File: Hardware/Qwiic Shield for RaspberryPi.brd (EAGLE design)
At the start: 65 x 30.5 mm, 24 parts, among them J1 Qwiic Right Angle, J10 RASPBERRYPI-40-PIN-GPIO_PTH_N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, J6 Qwiic Right Angle, J7 Qwiic Right Angle, J8 Qwiic Right Angle, U2 3.3V/600mA

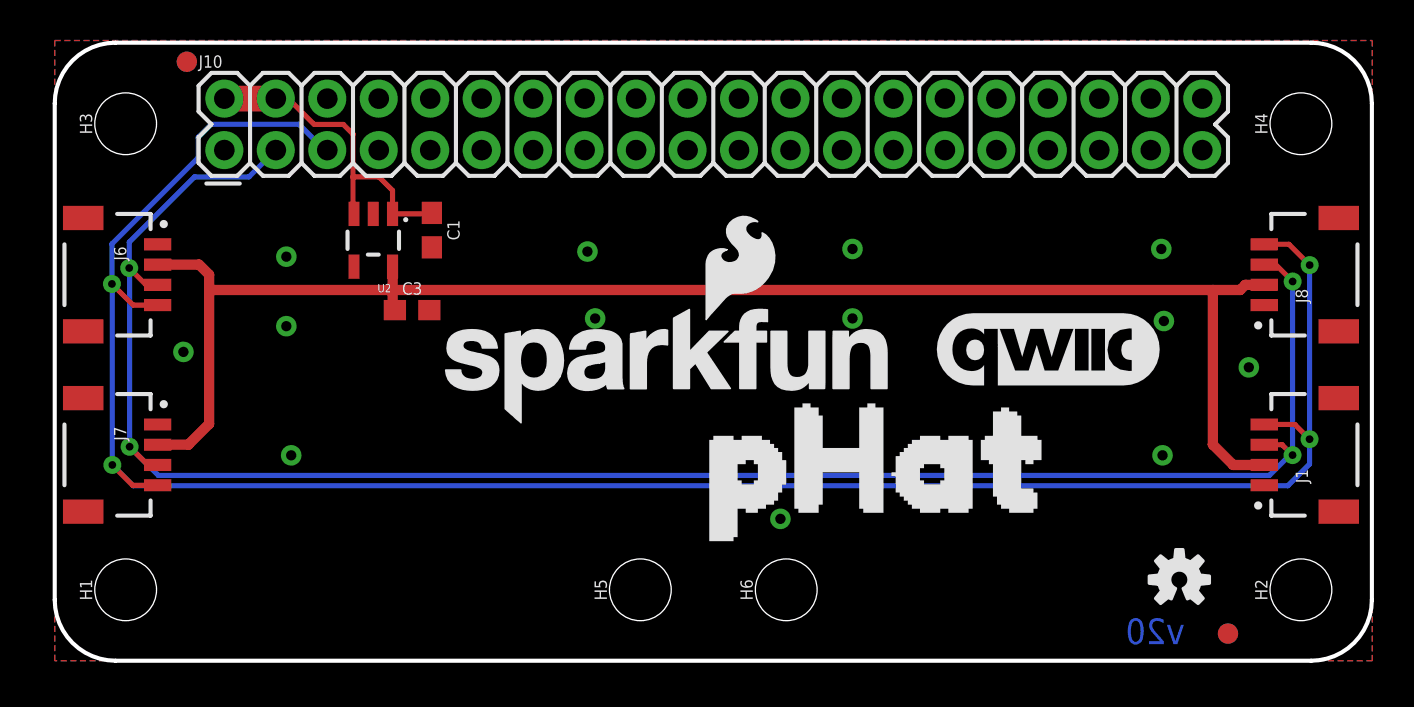
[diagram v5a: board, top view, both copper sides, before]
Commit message: Adds I2C pullup resistors
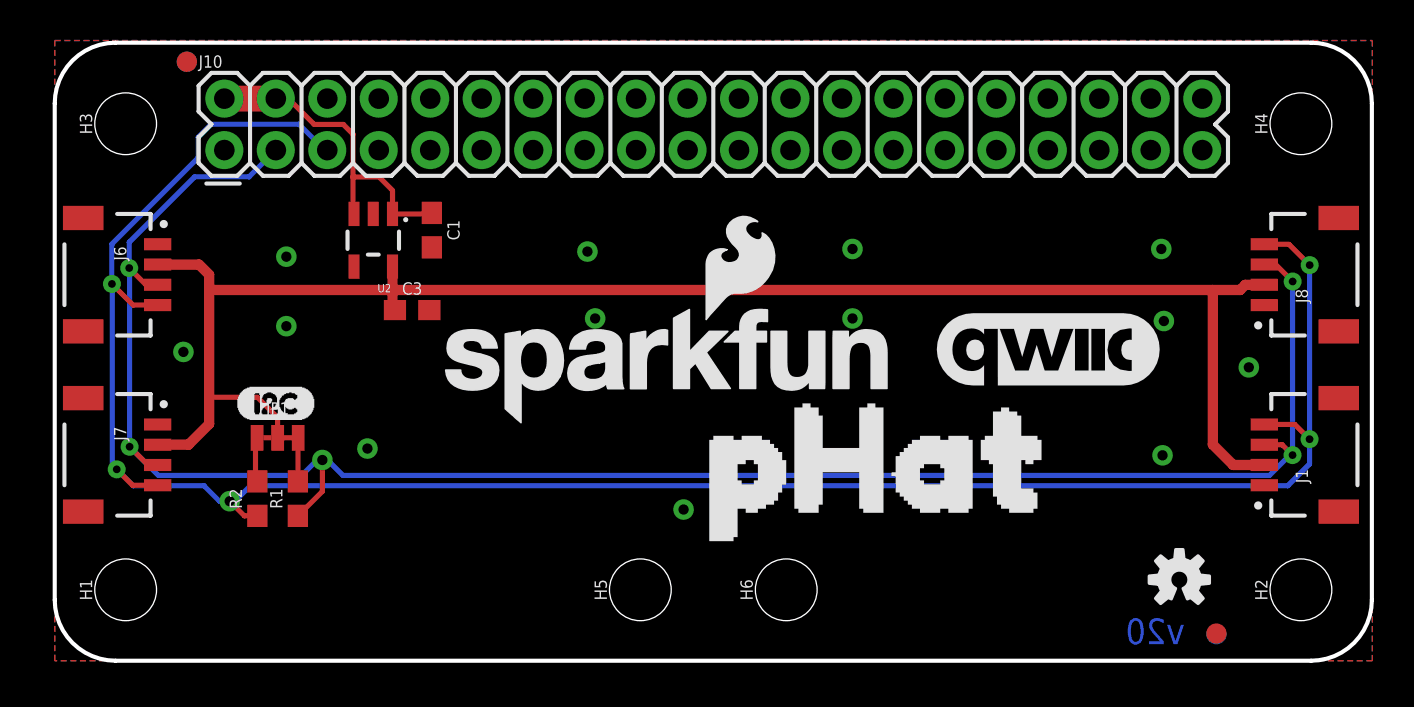
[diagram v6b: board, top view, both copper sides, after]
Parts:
- added JP1: PULLUP, SparkFun-Jumpers:SMT-JUMPER_3_2-NC_TRACE_NO-SILK
- added R1, R2: 2.2k, SparkFun-Resistors:0603
- added U$2: (no value), Labels:I2C-()
- moved FD3 0.57 mm to (57.3, 1.31)
- moved FD2 0.57 mm to (57.3, 1.34)
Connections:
- new net N$3: JP1.3, R1.2
- new net N$4: JP1.1, R2.2
- net 3.3V: now also JP1.2
- net SCL: now also R2.1
- net SDA: now also R1.1
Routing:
- net 3.3V: track 78.0 -> 82.8 mm
- net SDA: track 93.0 -> 97.1 mm, vias 4 -> 5
- net N$3: track 0.00 -> 2.57 mm
- net N$4: track 0.00 -> 2.32 mm
- net SCL: track 105.4 -> 107.4 mm, vias 4 -> 5
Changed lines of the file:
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@@
 <setting verticaltext="up"/>
 </settings>
-<grid distance="1" unitdist="mm" unit="mm" style="lines" multiple="1" display="yes" altdistance="0.01" altunitdist="mm" altunit="mm"/>
+<grid distance="0.1" unitdist="inch" unit="inch" style="lines" multiple="1" display="yes" altdistance="0.01" altunitdist="inch" altunit="inch"/>
 <layers>
 <layer number="1" name="Top" color="4" fill="1" visible="yes" active="yes"/>
@@
 </element>
 <element name="FD1" library="SparkFun-Aesthetics" package="FIDUCIAL-1X2" value="FIDUCIAL1X2" x="6.52" y="29.56" smashed="yes" rot="R180"/>
-<element name="FD2" library="SparkFun-Aesthetics" package="FIDUCIAL-1X2" value="FIDUCIAL1X2" x="57.9" y="1.34" smashed="yes" rot="R180"/>
+<element name="FD2" library="SparkFun-Aesthetics" package="FIDUCIAL-1X2" value="FIDUCIAL1X2" x="57.33" y="1.34" smashed="yes" rot="R180"/>
 <element name="J1" library="SparkFun-Connectors" package="JST04_1MM_RA" value="Qwiic Right Angle" x="59.68988125" y="10.16078125" smashed="yes" rot="R90">
 <attribute name="NAME" x="61.84888125" y="8.76378125" size="0.6096" layer="25" font="vector" ratio="20" rot="R90"/>
@@
 <attribute name="VALUE" x="62.992" y="17.399" size="0.6096" layer="27" font="vector" ratio="20" rot="R90"/>
 </element>
-<element name="FD3" library="SparkFun-Aesthetics" package="FIDUCIAL-1X2" value="FIDUCIAL1X2" x="57.9" y="1.34" smashed="yes" rot="MR0"/>
+<element name="FD3" library="SparkFun-Aesthetics" package="FIDUCIAL-1X2" value="FIDUCIAL1X2" x="57.33" y="1.31" smashed="yes" rot="MR0"/>
 <element name="FD4" library="SparkFun-Aesthetics" package="FIDUCIAL-1X2" value="FIDUCIAL1X2" x="6.52" y="29.56" smashed="yes" rot="MR0"/>
 <element name="LOGO2" library="SparkFun-Aesthetics" package="REVISION" value="REVISION" x="2.54" y="-26.67" smashed="yes"/>
@@
 <element name="LOGO3" library="SparkFun-Aesthetics" package="OSHW-LOGO-S" value="OSHW-LOGOS" x="55.5" y="4" smashed="yes"/>
 <element name="U$3" library="MicroPiHat" package="PHAT0" value="" x="27.5" y="10" smashed="yes"/>
+<element name="JP1" library="SparkFun-Jumpers" package="SMT-JUMPER_3_2-NC_TRACE_NO-SILK" value="PULLUP" x="11" y="11" smashed="yes">
+<attribute name="NAME" x="11" y="12.143" size="0.6096" layer="25" font="vector" ratio="20" align="bottom-center"/>
+<attribute name="VALUE" x="11" y="9.857" size="0.6096" layer="27" font="vector" ratio="20" align="top-center"/>
+</element>
+<element name="R1" library="SparkFun-Resistors" package="0603" value="2.2k" x="12" y="8" smashed="yes" rot="R90">
+<attribute name="NAME" x="11.238" y="8" size="0.6096" layer="25" font="vector" ratio="20" rot="R90" align="bottom-center"/>
+<attribute name="PROD_ID" value="RES-08272" x="12" y="8" size="1.778" layer="27" font="vector" ratio="15" rot="R90" display="off"/>
+<attribute name="VALUE" x="12.762" y="8" size="0.6096" layer="27" font="vector" ratio="20" rot="R90" align="top-center"/>
+</element>
+<element name="R2" library="SparkFun-Resistors" package="0603" value="2.2k" x="10" y="8" smashed="yes" rot="R90">
+<attribute name="NAME" x="9.238" y="8" size="0.6096" layer="25" font="vector" ratio="20" rot="R90" align="bottom-center"/>
+<attribute name="PROD_ID" value="RES-08272" x="10" y="8" size="1.778" layer="27" font="vector" ratio="15" rot="R90" display="off"/>
+<attribute name="VALUE" x="10.762" y="8" size="0.6096" layer="27" font="vector" ratio="20" rot="R90" align="top-center"/>
+</element>
+<element name="U$2" library="Labels" package="I2C-()" value="" x="8.89" y="12.7" smashed="yes"/>
 </elements>
 <signals>
@@
 <via x="39.37" y="16.891" extent="1-16" drill="0.508"/>
 <via x="39.37" y="20.32" extent="1-16" drill="0.508"/>
-<via x="11.67" y="10.137" extent="1-16" drill="0.508"/>
-<via x="35.813" y="7.002" extent="1-16" drill="0.508"/>
+<via x="15.432" y="10.471" extent="1-16" drill="0.508"/>
+<via x="31.033" y="7.462" extent="1-16" drill="0.508"/>
 <via x="54.67" y="10.137" extent="1-16" drill="0.508"/>
 </signal>
@@
 <wire x1="7.12" y1="19.55" x2="7.62" y2="19.05" width="0.508" layer="1"/>
 <wire x1="7.62" y1="19.05" x2="7.62" y2="18.296" width="0.508" layer="1"/>
-<wire x1="7.62" y1="18.296" x2="7.62" y2="11.684" width="0.508" layer="1"/>
+<wire x1="7.62" y1="18.296" x2="7.62" y2="13" width="0.508" layer="1"/>
+<wire x1="7.62" y1="13" x2="7.62" y2="11.684" width="0.508" layer="1"/>
 <wire x1="16.67" y1="18.296" x2="7.62" y2="18.296" width="0.508" layer="1"/>
 <wire x1="58.5" y1="18.296" x2="58.754" y2="18.55" width="0.508" layer="1"/>
 <wire x1="58.754" y1="18.55" x2="59.69" y2="18.55" width="0.508" layer="1"/>
+<contactref element="JP1" pad="2"/>
+<wire x1="11" y1="11" x2="11" y2="12" width="0.254" layer="1"/>
+<wire x1="11" y1="12" x2="10" y2="13" width="0.254" layer="1"/>
+<wire x1="10" y1="13" x2="7.62" y2="13" width="0.254" layer="1"/>
 </signal>
 <signal name="SDA">
@@
 <wire x1="3.6754" y1="20.6558" x2="3.6754" y2="19.3794" width="0.254" layer="16"/>
 <wire x1="3.6954" y1="10.5594" x2="5.1108" y2="9.144" width="0.254" layer="16"/>
-<wire x1="5.1108" y1="9.144" x2="59.944" y2="9.144" width="0.254" layer="16"/>
+<contactref element="R1" pad="1"/>
+<wire x1="12" y1="7.15" x2="11.85" y2="7.15" width="0.254" layer="1"/>
+<wire x1="5.1108" y1="9.144" x2="12.192" y2="9.144" width="0.254" layer="16"/>
+<wire x1="14.224" y1="9.144" x2="59.944" y2="9.144" width="0.254" layer="16"/>
+<wire x1="12" y1="7.15" x2="13.208" y2="8.358" width="0.254" layer="1"/>
+<wire x1="13.208" y1="8.358" x2="13.208" y2="9.906" width="0.254" layer="1"/>
+<via x="13.208" y="9.906" extent="1-16" drill="0.508"/>
+<wire x1="12.192" y1="9.144" x2="12.954" y2="9.906" width="0.254" layer="16"/>
+<wire x1="12.954" y1="9.906" x2="13.208" y2="9.906" width="0.254" layer="16"/>
+<wire x1="13.208" y1="9.906" x2="13.462" y2="9.906" width="0.254" layer="16"/>
+<wire x1="13.462" y1="9.906" x2="14.224" y2="9.144" width="0.254" layer="16"/>
 </signal>
 <signal name="SCL">
@@
 <contactref element="J8" pad="4"/>
 <contactref element="J10" pad="5"/>
-<via x="2.8426" y="9.6614" extent="1-16" drill="0.381"/>
 <wire x1="2.8226" y1="18.5952" x2="2.8426" y2="18.5752" width="0.254" layer="16"/>
 <wire x1="2.8426" y1="18.5752" x2="2.8426" y2="9.6614" width="0.254" layer="16"/>
@@
 <wire x1="60.9068" y1="20.55" x2="59.69" y2="20.55" width="0.254" layer="1"/>
 <wire x1="61.926" y1="10.9332" x2="61.926" y2="9.7062" width="0.254" layer="16"/>
-<wire x1="60.8558" y1="8.636" x2="3.868" y2="8.636" width="0.254" layer="16"/>
-<wire x1="2.8426" y1="9.6614" x2="3.868" y2="8.636" width="0.254" layer="16"/>
-<wire x1="61.926" y1="9.7062" x2="60.8558" y2="8.636" width="0.254" layer="16"/>
+<wire x1="2.8426" y1="9.6614" x2="3.059" y2="9.445" width="0.254" layer="16"/>
+<wire x1="3.059" y1="9.445" x2="3.868" y2="8.636" width="0.254" layer="16"/>
+<wire x1="60.8558" y1="8.636" x2="61.926" y2="9.7062" width="0.254" layer="16"/>
 <wire x1="2.8226" y1="18.5952" x2="2.8226" y2="20.5682" width="0.254" layer="16"/>
 <wire x1="12.049" y1="26.4768" x2="7.724" y2="26.4768" width="0.254" layer="16"/>
@@
 <wire x1="5.08" y1="17.55" x2="3.8678" y2="17.55" width="0.254" layer="1"/>
 <wire x1="3.8678" y1="17.55" x2="2.8226" y2="18.5952" width="0.254" layer="1"/>
-<wire x1="2.8426" y1="9.6614" x2="3.844" y2="8.66" width="0.254" layer="1"/>
-<wire x1="3.844" y1="8.66" x2="5.08" y2="8.66" width="0.254" layer="1"/>
 <wire x1="7.0794" y1="25.8322" x2="7.724" y2="26.4768" width="0.254" layer="16"/>
 <wire x1="2.8226" y1="20.5682" x2="7.0794" y2="24.825" width="0.254" layer="16"/>
 <wire x1="7.0794" y1="24.825" x2="7.0794" y2="25.8322" width="0.254" layer="16"/>
+<contactref element="R2" pad="1"/>
+<wire x1="5.08" y1="8.66" x2="3.844" y2="8.66" width="0.254" layer="1"/>
+<wire x1="3.844" y1="8.66" x2="3.059" y2="9.445" width="0.254" layer="1"/>
+<via x="3.059" y="9.445" extent="1-16" drill="0.381"/>
+<wire x1="3.868" y1="8.636" x2="7.366" y2="8.636" width="0.254" layer="16"/>
+<wire x1="7.366" y1="8.636" x2="8.128" y2="7.874" width="0.254" layer="16"/>
+<wire x1="8.128" y1="7.874" x2="8.636" y2="7.874" width="0.254" layer="16"/>
+<wire x1="8.636" y1="7.874" x2="8.89" y2="7.874" width="0.254" layer="16"/>
+<wire x1="8.89" y1="7.874" x2="9.652" y2="8.636" width="0.254" layer="16"/>
+<wire x1="9.652" y1="8.636" x2="60.8558" y2="8.636" width="0.254" layer="16"/>
+<via x="8.636" y="7.874" extent="1-16" drill="0.508"/>
+<wire x1="10" y1="7.15" x2="9.36" y2="7.15" width="0.254" layer="1"/>
+<wire x1="9.36" y1="7.15" x2="8.636" y2="7.874" width="0.254" layer="1"/>
 </signal>
 <signal name="5V">
@@
 <contactref element="J10" pad="1"/>
 </signal>
+<signal name="N$3">
+<contactref element="JP1" pad="3"/>
+<contactref element="R1" pad="2"/>
+<wire x1="12" y1="10.6229875" x2="12.0922" y2="10.7151875" width="0.254" layer="1"/>
+<wire x1="12.0922" y1="10.7151875" x2="12.0922" y2="11" width="0.254" layer="1"/>
+<wire x1="12.016" y1="11" x2="12" y2="10.984" width="0.254" layer="1"/>
+<wire x1="12" y1="10.984" x2="12" y2="8.85" width="0.254" layer="1"/>
+<wire x1="12.016" y1="11" x2="12.0922" y2="11" width="0" layer="19" extent="1-1"/>
+</signal>
+<signal name="N$4">
+<contactref element="JP1" pad="1"/>
+<contactref element="R2" pad="2"/>
+<wire x1="10" y1="10.6229875" x2="9.9078" y2="10.7151875" width="0.254" layer="1"/>
+<wire x1="9.9078" y1="10.7151875" x2="9.9078" y2="11" width="0.254" layer="1"/>
+<wire x1="9.9078" y1="8.9422" x2="9.9078" y2="10.7151875" width="0.254" layer="1"/>
+<wire x1="10" y1="8.85" x2="9.9078" y2="8.9422" width="0.254" layer="1"/>
+<wire x1="9.9078" y1="11" x2="9.984" y2="11" width="0" layer="19" extent="1-1"/>
+</signal>
 </signals>
